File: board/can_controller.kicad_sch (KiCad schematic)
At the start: 6 parts, among them U1 MCP2517FD-xSL, Y1 20MhZ

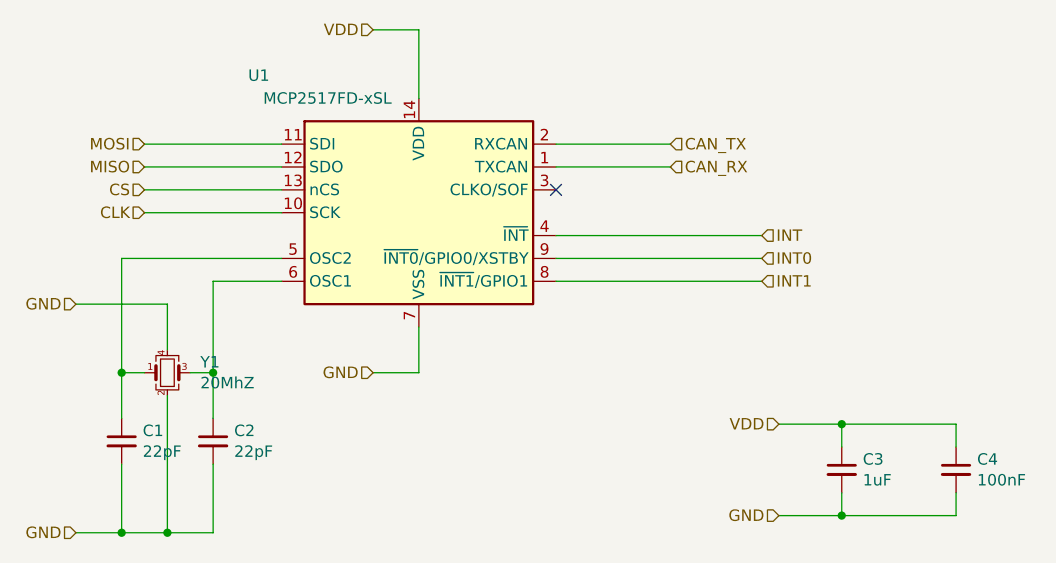
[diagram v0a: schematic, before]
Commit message: renamed subsheet to work better in compositions
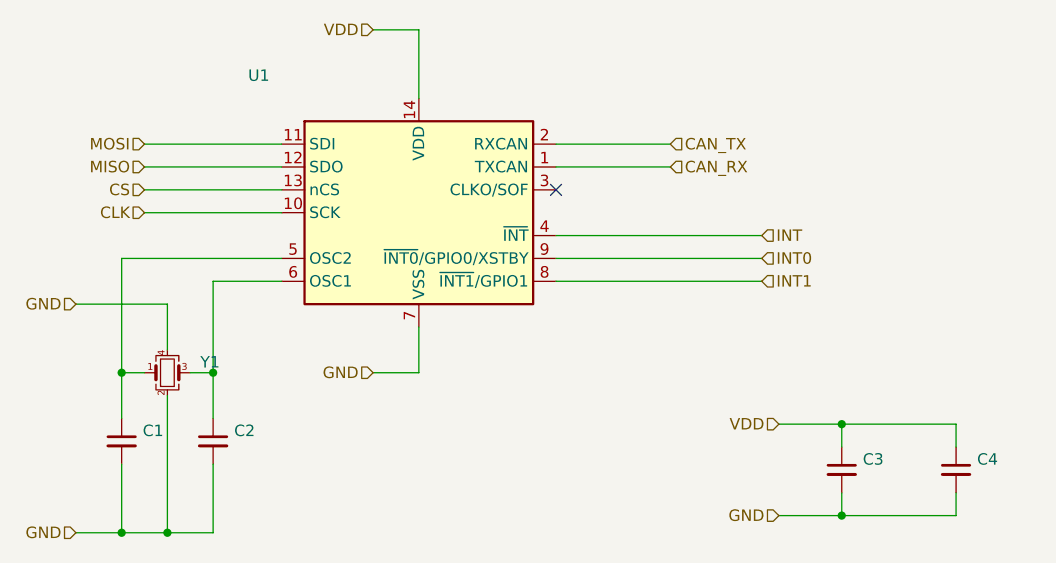
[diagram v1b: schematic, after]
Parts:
- C1, C2: value 22pF -> (none); footprint Capacitor_SMD:C_0603_1608Metric -> (none)
- C3: value 1uF -> (none); footprint Capacitor_SMD:C_0603_1608Metric -> (none)
- C4: value 100nF -> (none); footprint Capacitor_SMD:C_0603_1608Metric -> (none)
- U1: value MCP2517FD-xSL -> (none); footprint Package_SO:SOIC-14_3.9x8.7mm_P1.27mm -> (none)
- Y1: value 20MhZ -> (none); footprint Crystal:Crystal_SMD_Abracon_ABM8G-4Pin_3.2x2.5mm -> (none)
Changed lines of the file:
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@@
       (effects (font (size 1.27 1.27)) (justify left))
     )
-    (property "Value" "100nF" (id 1) (at 223.3168 122.428 0)
+    (property "Value" "" (id 1) (at 223.3168 122.428 0)
       (effects (font (size 1.27 1.27)) (justify left))
     )
-    (property "Footprint" "Capacitor_SMD:C_0603_1608Metric" (id 2) (at 220.98 121.285 0)
+    (property "Footprint" "" (id 2) (at 220.98 121.285 0)
       (effects (font (size 1.27 1.27)) hide)
     )
@@
       (effects (font (size 1.27 1.27)) (justify left))
     )
-    (property "Value" "20MhZ" (id 1) (at 137.0076 111.633 0)
+    (property "Value" "" (id 1) (at 137.0076 111.633 0)
       (effects (font (size 1.27 1.27)) (justify left))
     )
-    (property "Footprint" "Crystal:Crystal_SMD_Abracon_ABM8G-4Pin_3.2x2.5mm" (id 2) (at 133.35 110.49 0)
+    (property "Footprint" "" (id 2) (at 133.35 110.49 0)
       (effects (font (size 1.27 1.27)) hide)
     )
@@
       (effects (font (size 1.27 1.27)) (justify left))
     )
-    (property "Value" "1uF" (id 1) (at 210.6168 122.428 0)
+    (property "Value" "" (id 1) (at 210.6168 122.428 0)
       (effects (font (size 1.27 1.27)) (justify left))
     )
-    (property "Footprint" "Capacitor_SMD:C_0603_1608Metric" (id 2) (at 208.28 121.285 0)
+    (property "Footprint" "" (id 2) (at 208.28 121.285 0)
       (effects (font (size 1.27 1.27)) hide)
     )
@@
     (in_bom yes) (on_board yes)
     (property "Reference" "U1" (id 0) (at 143.51 77.47 0))
-    (property "Value" "MCP2517FD-xSL" (id 1) (at 151.13 80.01 0))
-    (property "Footprint" "Package_SO:SOIC-14_3.9x8.7mm_P1.27mm" (id 2) (at 161.29 118.11 0)
+    (property "Value" "" (id 1) (at 151.13 80.01 0))
+    (property "Footprint" "" (id 2) (at 161.29 118.11 0)
       (effects (font (size 1.27 1.27)) hide)
     )
@@
       (effects (font (size 1.27 1.27)) (justify left))
     )
-    (property "Value" "22pF" (id 1) (at 130.6068 119.253 0)
+    (property "Value" "" (id 1) (at 130.6068 119.253 0)
       (effects (font (size 1.27 1.27)) (justify left))
     )
-    (property "Footprint" "Capacitor_SMD:C_0603_1608Metric" (id 2) (at 128.27 118.11 0)
+    (property "Footprint" "" (id 2) (at 128.27 118.11 0)
       (effects (font (size 1.27 1.27)) hide)
     )
@@
       (effects (font (size 1.27 1.27)) (justify right))
     )
-    (property "Value" "22pF" (id 1) (at 140.7668 119.253 0)
+    (property "Value" "" (id 1) (at 140.7668 119.253 0)
       (effects (font (size 1.27 1.27)) (justify right))
     )
-    (property "Footprint" "Capacitor_SMD:C_0603_1608Metric" (id 2) (at 138.43 118.11 0)
+    (property "Footprint" "" (id 2) (at 138.43 118.11 0)
       (effects (font (size 1.27 1.27)) hide)
     )
